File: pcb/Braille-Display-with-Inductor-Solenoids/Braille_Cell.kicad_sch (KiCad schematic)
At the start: 15 parts, among them U2 TPIC6595

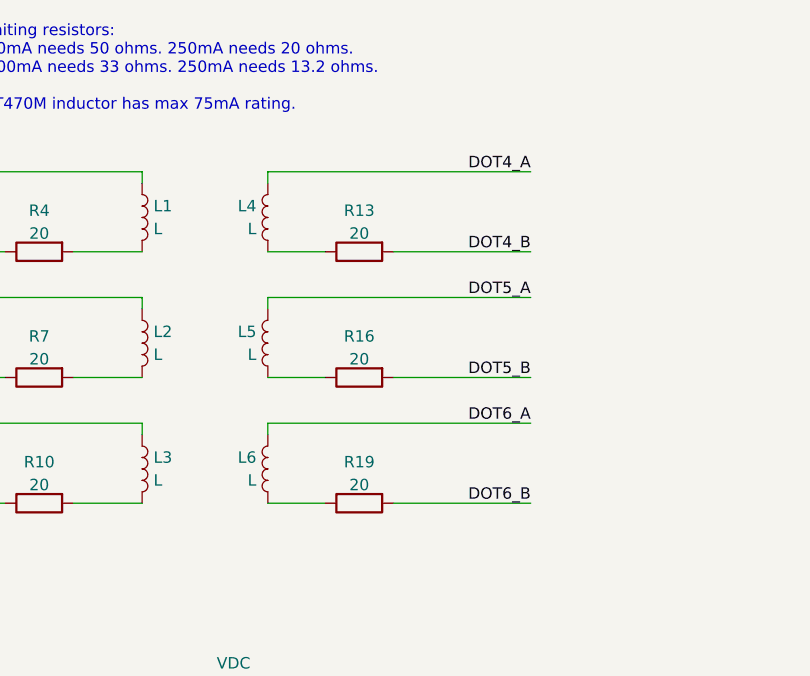
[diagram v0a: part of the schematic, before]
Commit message: Update net class rules for routing
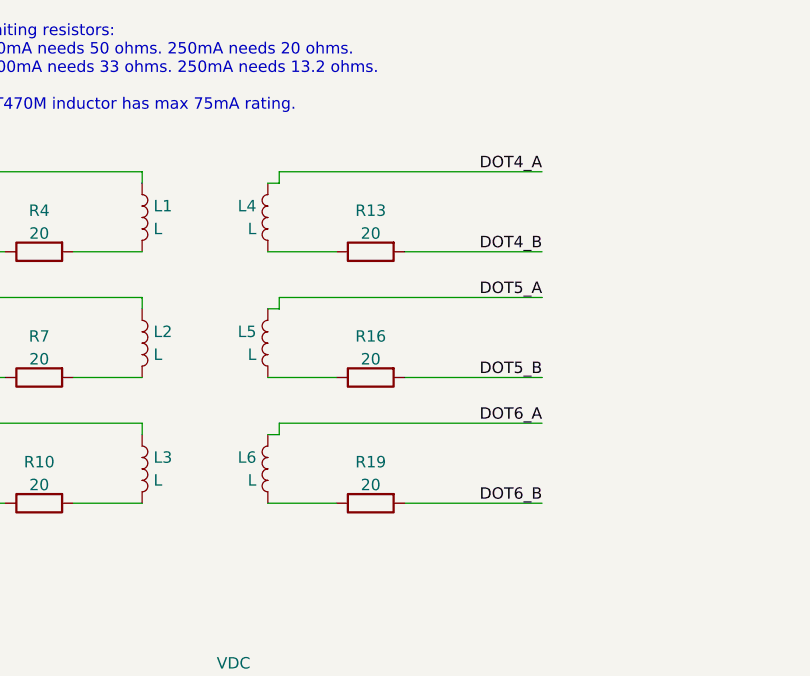
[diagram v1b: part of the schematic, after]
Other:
- moved on the sheet: R13, R16, R19

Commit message: Create flat inductor PCB
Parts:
- L1, L2, L3, L4, L5, L6: footprint 00-project-footprint-lib:Inductor_0805_2012Metric_SMD_Vertical_Square -> 00-project-footprint-lib:Inductor_VLS201612CX
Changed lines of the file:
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@@
 			)
 		)
-		(property "Footprint" "00-project-footprint-lib:Inductor_0805_2012Metric_SMD_Vertical_Square"
+		(property "Footprint" "00-project-footprint-lib:Inductor_VLS201612CX"
 			(at 107.95 66.04 0)
 			(effects
@@
 			)
 		)
-		(property "Footprint" "00-project-footprint-lib:Inductor_0805_2012Metric_SMD_Vertical_Square"
+		(property "Footprint" "00-project-footprint-lib:Inductor_VLS201612CX"
 			(at 107.95 52.07 0)
 			(effects
@@
 			)
 		)
-		(property "Footprint" "00-project-footprint-lib:Inductor_0805_2012Metric_SMD_Vertical_Square"
+		(property "Footprint" "00-project-footprint-lib:Inductor_VLS201612CX"
 			(at 121.92 66.04 0)
 			(effects
@@
 			)
 		)
-		(property "Footprint" "00-project-footprint-lib:Inductor_0805_2012Metric_SMD_Vertical_Square"
+		(property "Footprint" "00-project-footprint-lib:Inductor_VLS201612CX"
 			(at 107.95 38.1 0)
 			(effects
@@
 			)
 		)
-		(property "Footprint" "00-project-footprint-lib:Inductor_0805_2012Metric_SMD_Vertical_Square"
+		(property "Footprint" "00-project-footprint-lib:Inductor_VLS201612CX"
 			(at 121.92 38.1 0)
 			(effects
@@
 			)
 		)
-		(property "Footprint" "00-project-footprint-lib:Inductor_0805_2012Metric_SMD_Vertical_Square"
+		(property "Footprint" "00-project-footprint-lib:Inductor_VLS201612CX"
 			(at 121.92 52.07 0)
 			(effects
